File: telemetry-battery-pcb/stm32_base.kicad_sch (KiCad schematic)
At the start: 41 parts, among them J1 Network Connector, J2 STDC14, SW1 SW_Push, U1 LD39050PU33R, U2 STM32G474RBT6, U3 SN65HVD230, Y1 8MHz

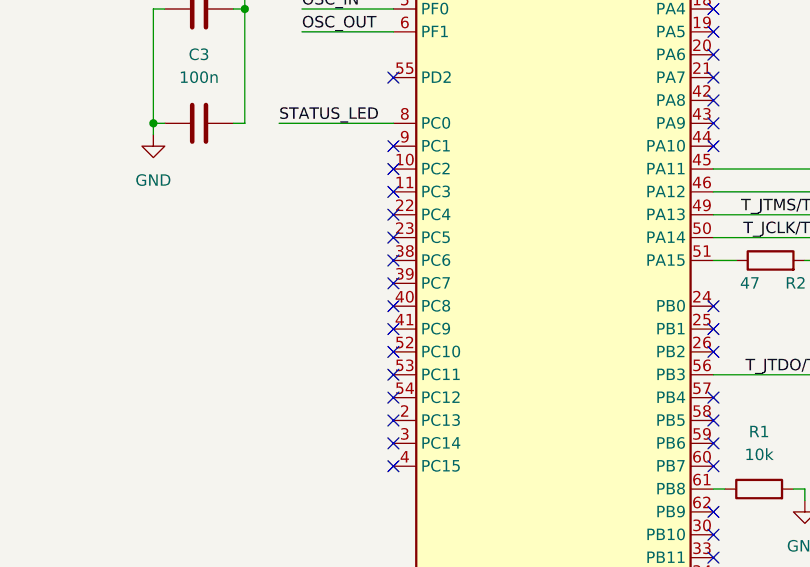
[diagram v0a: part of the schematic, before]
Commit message: telemetry-battery-pcb: complete LTC2944 circuitry
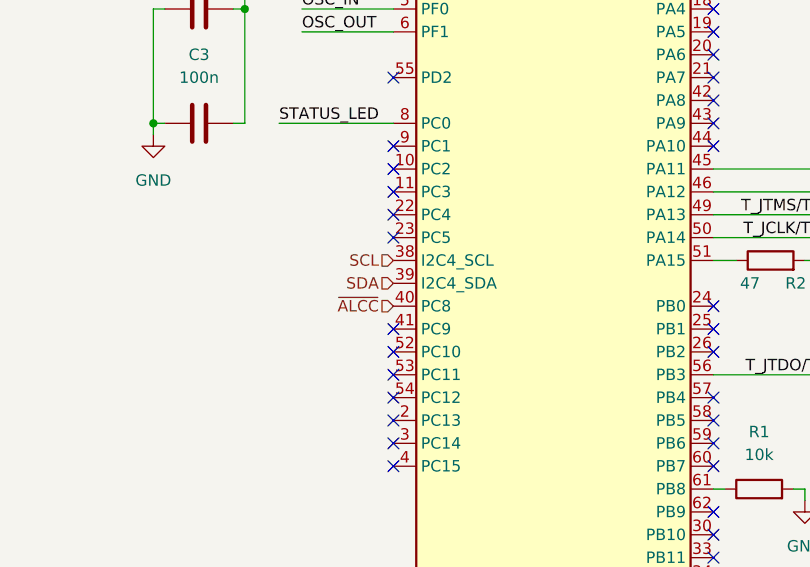
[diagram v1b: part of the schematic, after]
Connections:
- net SCL: now reaches U2.38 (PC6)
- net SDA: now reaches U2.39 (PC7)
- net ~{ALCC}: now reaches U2.40 (PC8)
- no-connect marks 42 -> 39
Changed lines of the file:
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@@
-	)
-	(no_connect
-		(at 63.5 138.43)
 	)
 	(no_connect
@@
 	)
 	(no_connect
-		(at 63.5 133.35)
-	)
-	(no_connect
 		(at 99.06 140.97)
 	)
@@
 	)
 	(no_connect
-		(at 63.5 135.89)
-	)
-	(no_connect
 		(at 99.06 113.03)
 	)
@@
 			)
 			(justify right bottom)
+		)
+	)
+	(hierarchical_label "SCL"
+		(shape input)
+		(at 63.5 133.35 180)
+		(effects
+			(font
+				(size 1.27 1.27)
+			)
+			(justify right)
+		)
+	)
+	(hierarchical_label "SDA"
+		(shape input)
+		(at 63.5 135.89 180)
+		(effects
+			(font
+				(size 1.27 1.27)
+			)
+			(justify right)
+		)
+	)
+	(hierarchical_label "~{ALCC}"
+		(shape input)
+		(at 63.5 138.43 180)
+		(effects
+			(font
+				(size 1.27 1.27)
+			)
+			(justify right)
 		)
 	)
@@
 		)
 		(pin "38"
+			(alternate "I2C4_SCL")
 		)
 		(pin "15"
@@
 		)
 		(pin "39"
+			(alternate "I2C4_SDA")
 		)
 		(pin "55"

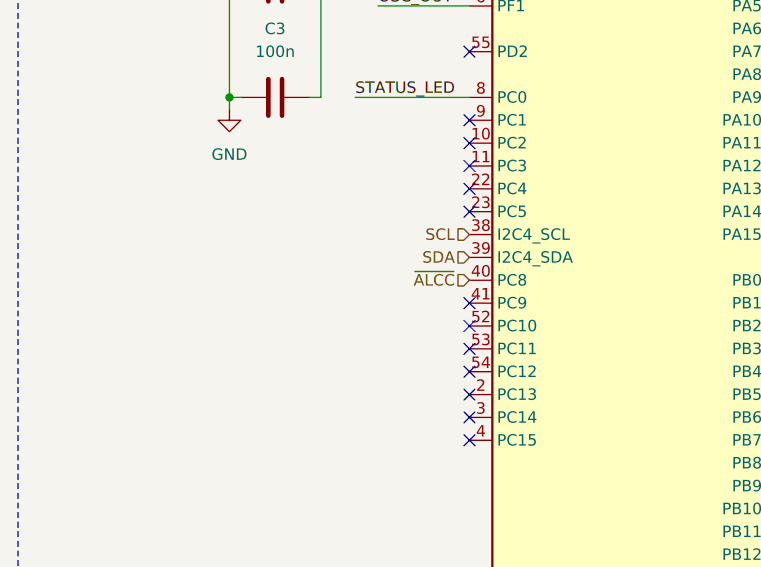
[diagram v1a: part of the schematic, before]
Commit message: telemetry-battery-pcb: corrections (battery gauge, EEPROM)
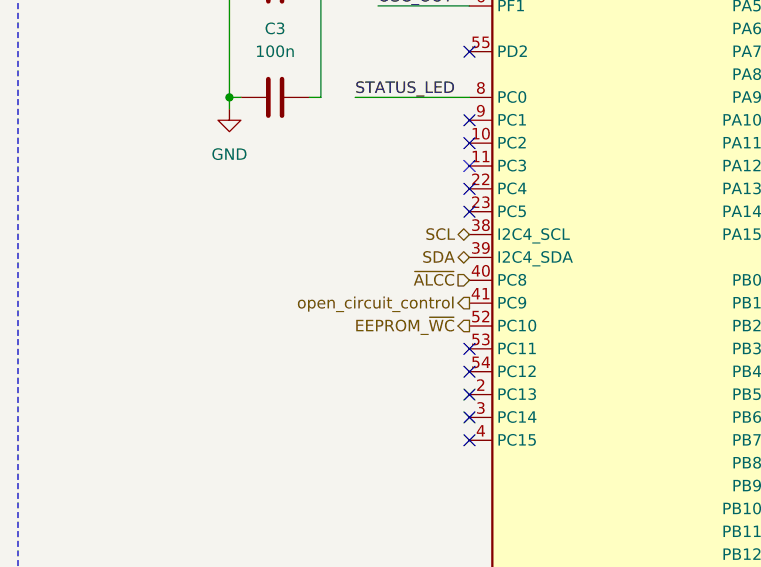
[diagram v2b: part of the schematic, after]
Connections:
- net open_circuit_control: now reaches U2.41 (PC9)
- net EEPROM_~{WC}: now reaches U2.52 (PC10)
- no-connect marks 39 -> 37
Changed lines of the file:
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@@
-	)
-	(no_connect
-		(at 63.5 143.51)
 	)
 	(no_connect
@@
 	(no_connect
 		(at 63.5 113.03)
-	)
-	(no_connect
-		(at 63.5 140.97)
 	)
 	(no_connect
@@
 	)
 	(hierarchical_label "SCL"
-		(shape input)
+		(shape bidirectional)
 		(at 63.5 133.35 180)
 		(effects
@@
 	)
 	(hierarchical_label "SDA"
-		(shape input)
+		(shape bidirectional)
 		(at 63.5 135.89 180)
 		(effects
@@
 		(effects
 			(font
+				(size 1.27 1.27)
+			)
+			(justify right)
+		)
+	)
+	(hierarchical_label "EEPROM_~{WC}"
+		(shape output)
+		(at 63.5 143.51 180)
+		(effects
+			(font
+				(size 1.27 1.27)
+			)
+			(justify right)
+		)
+	)
+	(hierarchical_label "open_circuit_control"
+		(shape output)
+		(at 63.5 140.97 180)
+		(effects
+			(font

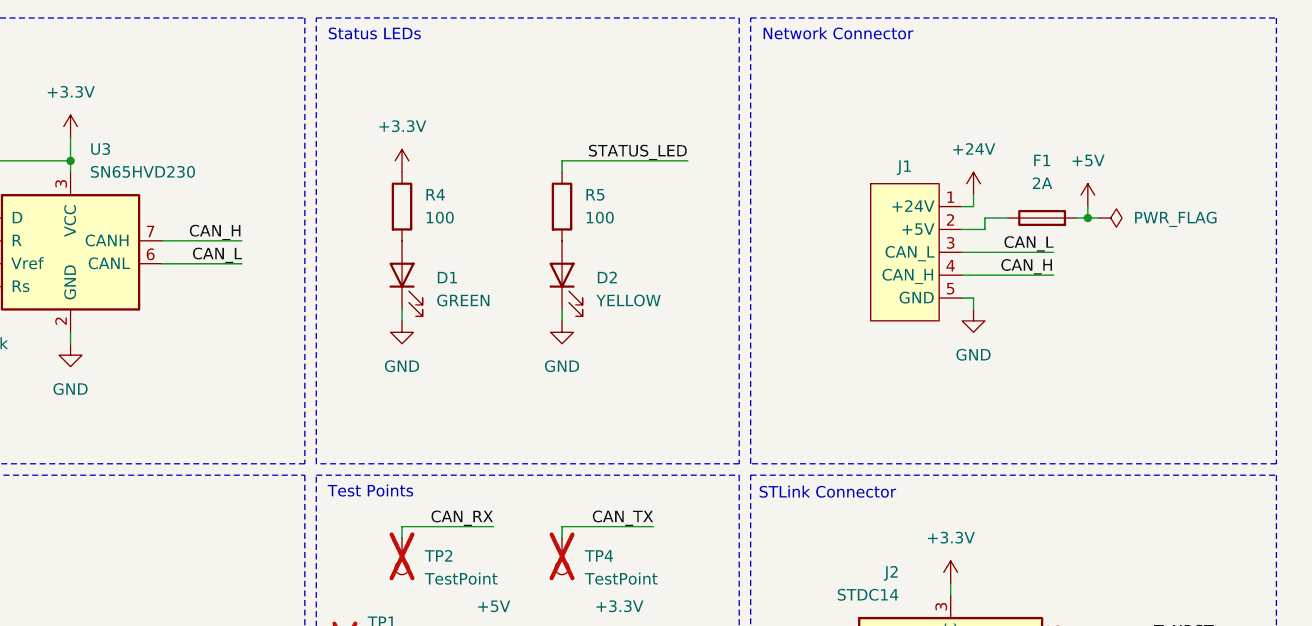
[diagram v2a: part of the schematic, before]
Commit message: telemetry-battery-pcb: add MOSFETs & change DC-DC Converter 24V->5V (TPSM86837)
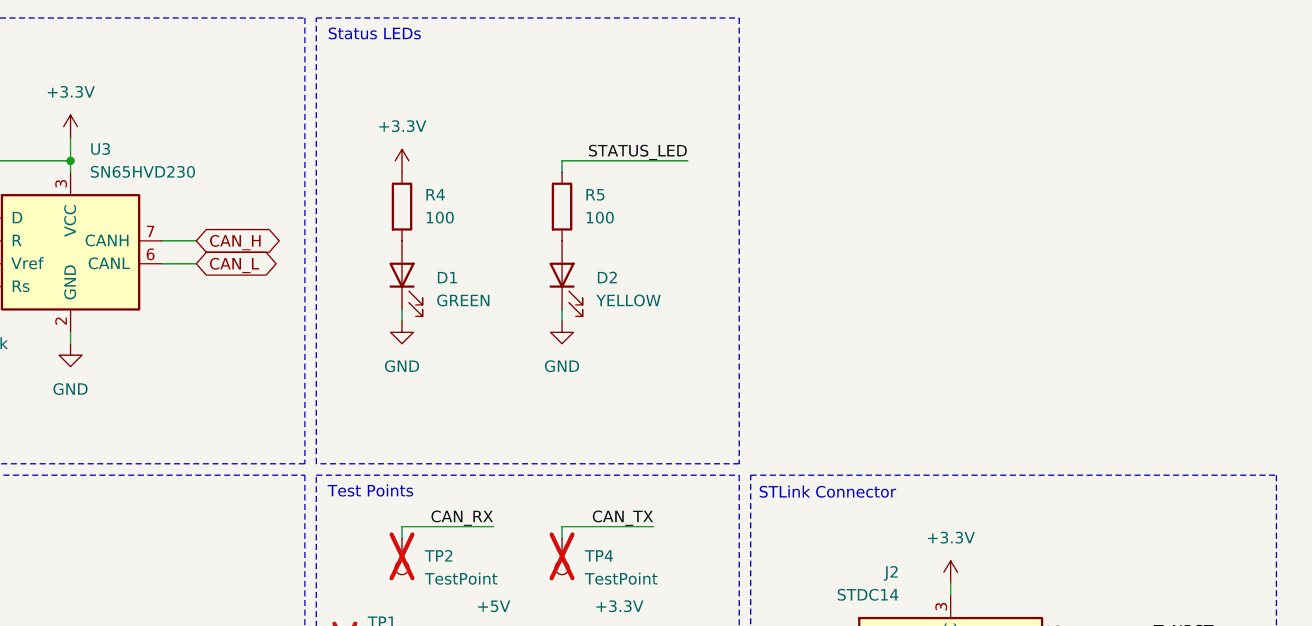
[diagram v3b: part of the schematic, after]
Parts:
- removed F1: 2A, Exocet:Fuse_Holder_Littelfuse_01530008, symbol Device:Fuse
- removed J1: Network Connector, Connector_Molex:Molex_SPOX_5268-05A_1x05_P2.50mm_Horizontal, symbol Exocet:Network_Connector
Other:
- note removed: "Network Connector"

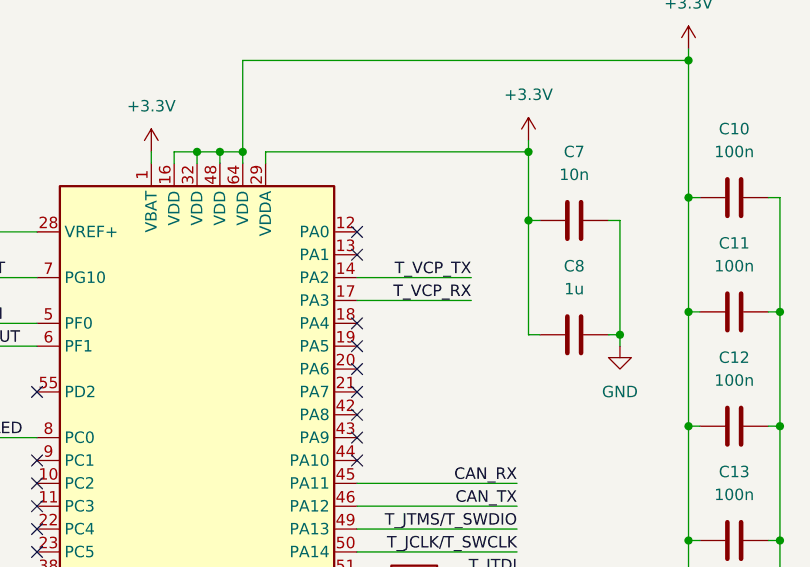
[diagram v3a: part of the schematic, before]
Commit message: telemetry-battery-pcb: connections for  TPS1HTC30-Q1
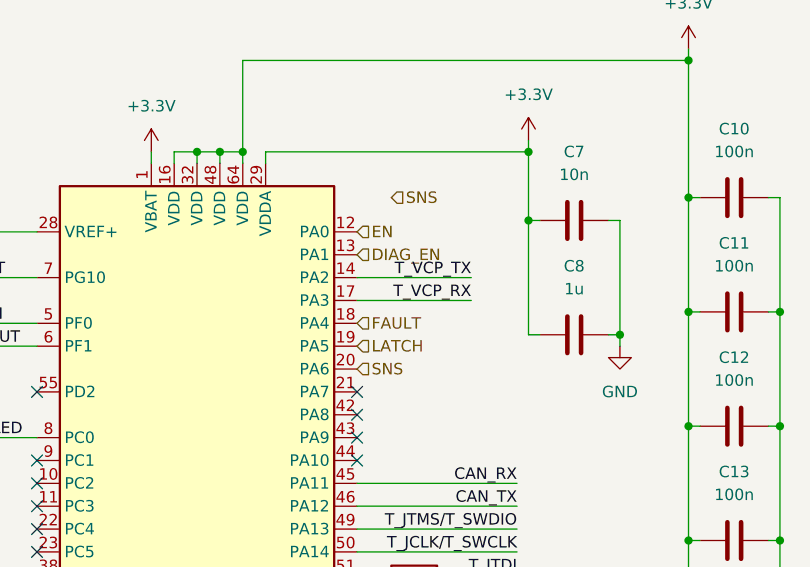
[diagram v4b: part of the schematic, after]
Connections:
- net EN: now reaches U2.12 (PA0)
- net DIAG_EN: now reaches U2.13 (PA1)
- net FAULT: now reaches U2.18 (PA4)
- net LATCH: now reaches U2.19 (PA5)
- net SNS: now reaches U2.20 (PA6)
- no-connect marks 37 -> 32
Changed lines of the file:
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@@
-	)
-	(no_connect
-		(at 99.06 110.49)
 	)
 	(no_connect
@@
 	)
 	(no_connect
-		(at 99.06 107.95)
-	)
-	(no_connect
 		(at 99.06 148.59)
 	)
@@
 	)
 	(no_connect
-		(at 99.06 97.79)
-	)
-	(no_connect
 		(at 63.5 120.65)
 	)
 	(no_connect
-		(at 99.06 95.25)
-	)
-	(no_connect
 		(at 63.5 130.81)
 	)
@@
 	(no_connect
 		(at 63.5 123.19)
-	)
-	(no_connect
-		(at 99.06 105.41)
 	)
 	(no_connect
@@
 		)
 	)
+	(hierarchical_label "DIAG_EN"
+		(shape input)
+		(at 99.06 97.79 0)
+		(effects
+			(font
+				(size 1.27 1.27)
+			)
+			(justify left)
+		)
+	)
 	(hierarchical_label "~{ALCC}"
 		(shape input)
@@
 		)
 	)
+	(hierarchical_label "EN"
+		(shape input)
+		(at 99.06 95.25 0)
+		(effects
+			(font
+				(size 1.27 1.27)
+			)
+			(justify left)
+		)
+	)
+	(hierarchical_label "LATCH"
+		(shape input)
+		(at 99.06 107.95 0)
+		(effects
+			(font
+				(size 1.27 1.27)
+			)
+			(justify left)
+		)
+	)
+	(hierarchical_label "SNS"
+		(shape input)
+		(at 99.06 110.49 0)
+		(effects
+			(font
+				(size 1.27 1.27)
+			)
+			(justify left)
+		)
+	)
+	(hierarchical_label "SNS"
+		(shape input)
+		(at 102.87 91.44 0)
+		(effects
+			(font
+				(size 1.27 1.27)
+			)
+			(justify left)
+		)
+	)
+	(hierarchical_label "FAULT"
+		(shape input)
+		(at 99.06 105.41 0)
+		(effects
+			(font
+				(size 1.27 1.27)
+			)
+			(justify left)
+		)
+	)

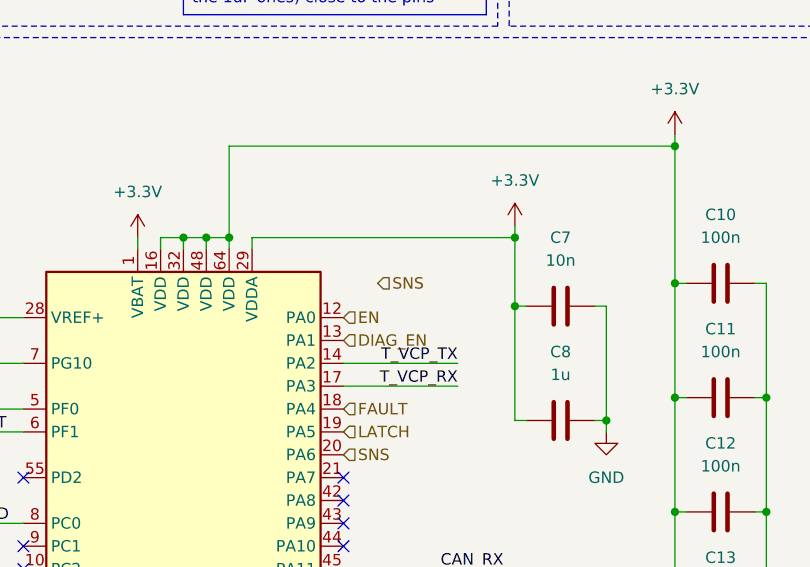
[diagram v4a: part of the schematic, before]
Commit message: telemetry-battery-pcb: schematic connections complete
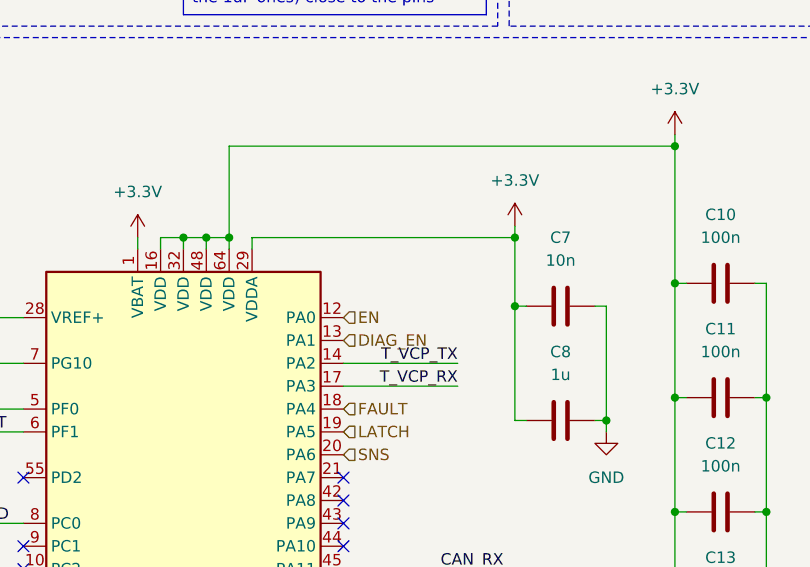
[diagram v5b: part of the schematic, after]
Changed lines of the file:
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@@
-		)
-	)
-	(hierarchical_label "SNS"
-		(shape input)
-		(at 102.87 91.44 0)
-		(effects
-			(font
-				(size 1.27 1.27)
-			)
-			(justify left)
 		)
 	)

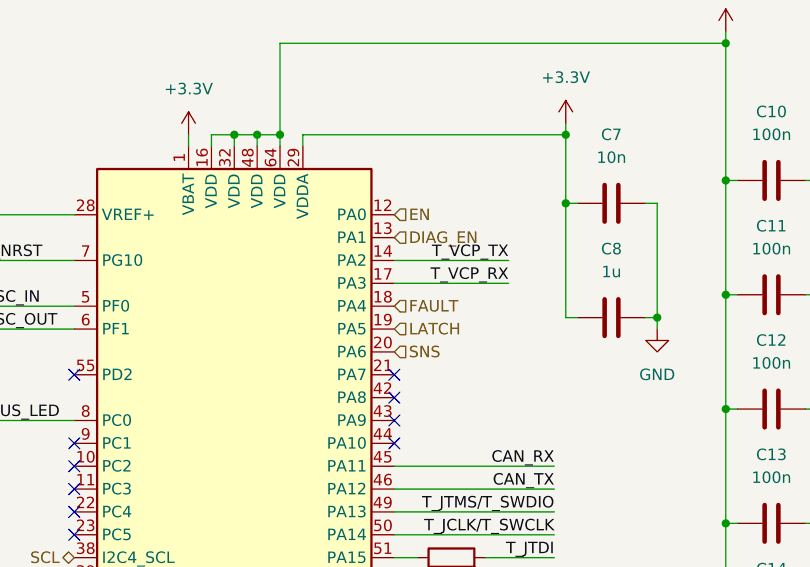
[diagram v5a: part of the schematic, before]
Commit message: telemetry-battery-pcb: review schematic and pcb
Changes:
- Reduce the value of fuse F2 to 10A (no impact on footprint or JLCPCB
  number)
- Group all test points together (and relevant changes to PCB)
  - +24V test point
  - I2C test points (SDA and SCL)
- Change the 24V-network used as input for the 5V DC-DC (and relevant
  changes to PCB). The STM32 on this PCB needs to be powered on (using
  the 5V-network) in ordrer to enable the 24V-net output for other PCBs.
  Therefore, the DC-DC converter needs to be supplied directly from the
  battery, as described in the TPS1HTC30 datasheet.
- Change the position of the +5V power label (and relevant changes to
  PCB). The reasoning is similar to the previous point. The 5V_NET is
  controlled by the STM32 itself, which therefore needs to be powered on
  separately.
- Change the 24V-network used for the PGOOD LED (results from changing
  the 24V-nework input to the DC-DC converter). PCB was also updated to
  reflect these changes.
- Connect the TPS1HTC30 I/O to STM32. There was an incompatibility with
  the labels used which meant KiCad didn't properly connect the nets.
  Now we have local labels in the root page, connected to hierarchical
  labels from the STM32-page. Also swapped the pin used by SNS to PA0,
  since it needs to be connected to an ADC (PA0 is input 1 of ADC 1).
  PCB was NOT updated accordingly.
- Reorganize and cleaned some labels and text in the schematic
  (alignment, etc.) for clarity.
- Change the style of the DC-DC converter's pin 1 dot in the footprint.
  Also added traces between the inernally connected pins to remove the
  DRC warnings.
- Update PCB metadata (name, code, authors, reviewers, etc.). Also
  updated the text in the Silkscreen for the name of the pcb to match
  what there is in the template.
- Simplify routing in the PCB and removed redundant traces
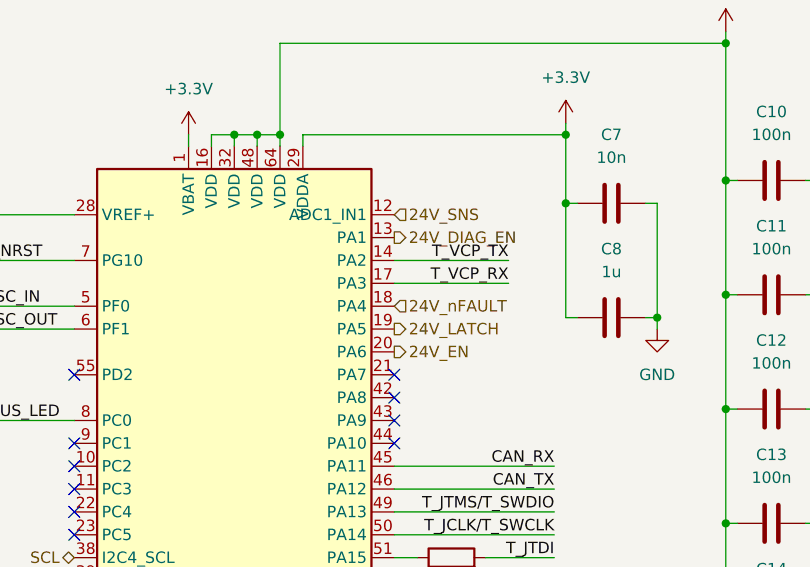
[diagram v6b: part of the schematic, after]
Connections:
- net DIAG_EN renamed 24V_DIAG_EN
- net EN renamed 24V_SNS
- net FAULT renamed 24V_nFAULT
- net LATCH renamed 24V_LATCH
- net SNS renamed 24V_EN
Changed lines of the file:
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@@
 		)
 	)
-	(hierarchical_label "DIAG_EN"
-		(shape input)
+	(hierarchical_label "24V_DIAG_EN"
+		(shape output)
 		(at 99.06 97.79 0)
 		(effects
@@
 		)
 	)
-	(hierarchical_label "EN"
-		(shape input)
-		(at 99.06 95.25 0)
+	(hierarchical_label "24V_EN"
+		(shape output)
+		(at 99.06 110.49 0)
 		(effects
 			(font
@@
 		)
 	)
-	(hierarchical_label "LATCH"
-		(shape input)
+	(hierarchical_label "24V_LATCH"
+		(shape output)
 		(at 99.06 107.95 0)
 		(effects
@@
 		)
 	)
-	(hierarchical_label "SNS"
-		(shape input)
-		(at 99.06 110.49 0)
-		(effects
-			(font
-				(size 1.27 1.27)
-			)
-			(justify left)
-		)
-	)
-	(hierarchical_label "FAULT"
+	(hierarchical_label "24V_nFAULT"
 		(shape input)
 		(at 99.06 105.41 0)
@@
 		)
 	)
+	(hierarchical_label "24V_SNS"
+		(shape input)
+		(at 99.06 95.25 0)
+		(effects
+			(font
+				(size 1.27 1.27)
+			)
+			(justify left)
+		)
+	)
 	(hierarchical_label "open_circuit_control"
 		(shape output)
@@
 		)
 		(pin "12"
+			(alternate "ADC1_IN1")
 		)
 		(pin "41"

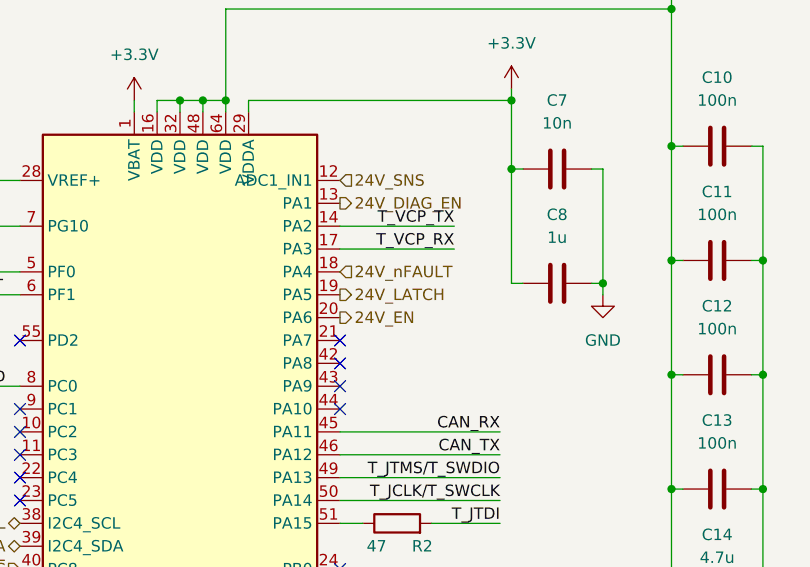
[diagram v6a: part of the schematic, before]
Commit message: telemetry-battery-pcb: move certains traces and vias
Swapped nFAULT and LATCH signals to avoid vias on one of them. Removed
90-degree corners on some traces. Move fuse for shorter traces.
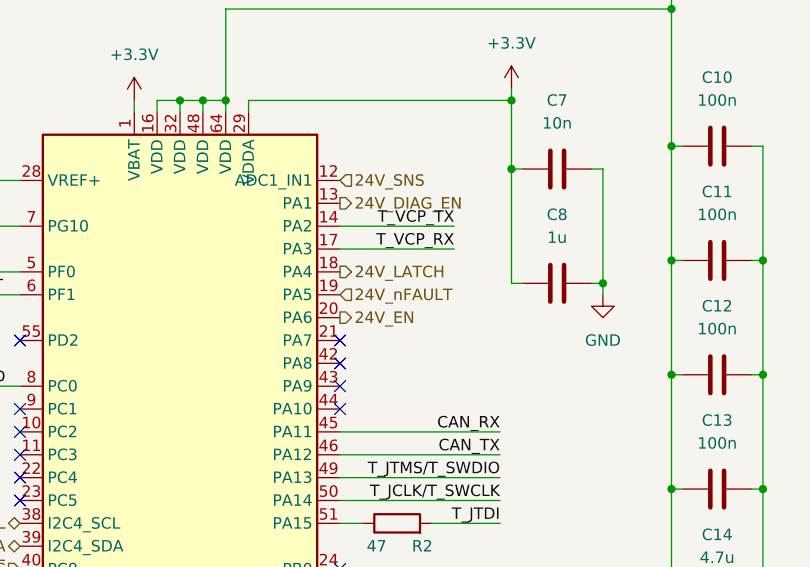
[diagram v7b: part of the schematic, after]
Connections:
- net 24V_LATCH: now also U2.18 (PA4); no longer U2.19 (PA5)
- net 24V_nFAULT: now also U2.19 (PA5); no longer U2.18 (PA4)
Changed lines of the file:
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@@
+		)
+	)
+	(hierarchical_label "24V_nFAULT"
+		(shape input)
+		(at 99.06 107.95 0)
+		(effects
+			(font
+				(size 1.27 1.27)
+			)
+			(justify left)
 		)
 	)
@@
 	(hierarchical_label "24V_LATCH"
 		(shape output)
-		(at 99.06 107.95 0)
-		(effects
-			(font
-				(size 1.27 1.27)
-			)
-			(justify left)
-		)
-	)
-	(hierarchical_label "24V_nFAULT"
-		(shape input)
 		(at 99.06 105.41 0)
 		(effects
